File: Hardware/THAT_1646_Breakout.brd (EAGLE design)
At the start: 45.7 x 20.3 mm, 28 parts, among them IC1 THAT1646, J1 1x4, J2 SN, J3 CHASSIS, J4 TN, J5 RN, J6 OUTPUT

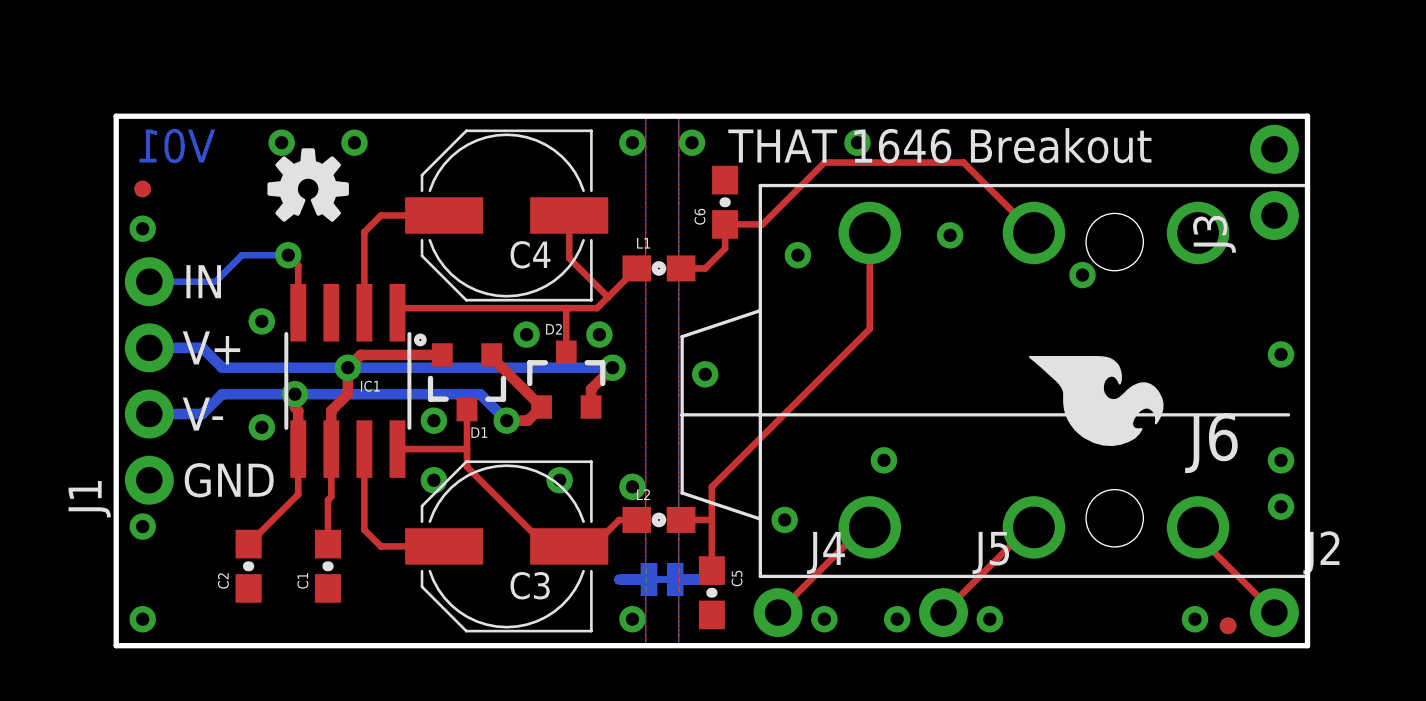
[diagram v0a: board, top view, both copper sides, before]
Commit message: Adding testpoints on T/R/S connections.
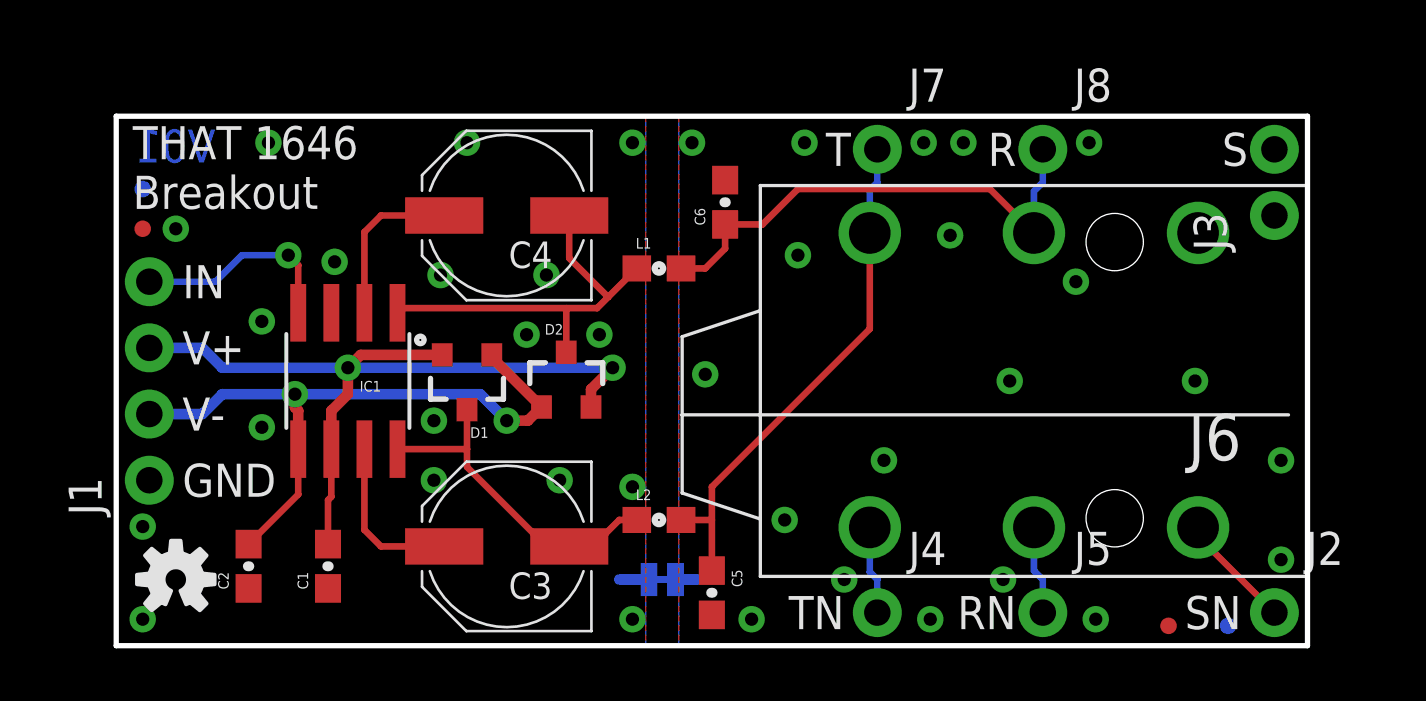
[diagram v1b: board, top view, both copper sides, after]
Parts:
- removed LOGO3: SFE_LOGO_FLAME.2_INCH, SparkFun-Aesthetics:SFE_LOGO_FLAME_.2
- added J7: T, SparkFun-Connectors:1X01_NO_SILK
- added J8: R, SparkFun-Connectors:1X01_NO_SILK
- moved LOGO5 22.4 mm to (17.9, 14.7)
- moved LOGO1 15.8 mm to (2.29, 2.54)
- moved J4 3.81 mm to (29.2, 1.27)
- moved J5 3.81 mm to (35.6, 1.27)
- moved LOGO2 3.39 mm to (4.06, 16.8)
- moved FD4 2.29 mm to (40.4, 0.76)
- moved FD3 1.52 mm to (1.02, 16.0)
- moved LOGO4 1.27 mm to (34.8, 8.64)
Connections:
- net N$8: now also J7.1
- net N$9: now also J8.1
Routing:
- net N$8: track 16.7 -> 20.0 mm
- net N$9: track 16.9 -> 19.4 mm
- net N$2: track 4.87 -> 3.39 mm
- net N$1: track 4.82 -> 3.41 mm
- net GND-ISO: vias 15 -> 20
- net GND: vias 15 -> 18
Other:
- board text added: "R"
- board text added: "S"
- board text added: "T"

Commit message: Moving PTH holes to 0.1 grid.
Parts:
- moved J5 1.27 mm to (36.8, 1.27)
- moved J8 1.27 mm to (36.8, 19.1)
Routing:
- net N$9: track 19.4 -> 19.9 mm
- net N$1: track 3.41 -> 3.94 mm
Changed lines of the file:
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@@
 <setting verticaltext="up"/>
 </settings>
-<grid distance="0.1" unitdist="inch" unit="inch" style="lines" multiple="1" display="yes" altdistance="0.01" altunitdist="inch" altunit="inch"/>
+<grid distance="0.05" unitdist="inch" unit="inch" style="lines" multiple="1" display="yes" altdistance="0.005" altunitdist="inch" altunit="inch"/>
 <layers>
 <layer number="1" name="Top" color="4" fill="1" visible="yes" active="yes"/>
@@
 <layer number="22" name="bPlace" color="14" fill="1" visible="yes" active="yes"/>
 <layer number="23" name="tOrigins" color="15" fill="1" visible="yes" active="yes"/>
-<layer number="24" name="bOrigins" color="15" fill="1" visible="no" active="yes"/>
-<layer number="25" name="tNames" color="7" fill="1" visible="yes" active="yes"/>
+<layer number="24" name="bOrigins" color="15" fill="1" visible="yes" active="yes"/>
+<layer number="25" name="tNames" color="7" fill="1" visible="no" active="yes"/>
 <layer number="26" name="bNames" color="7" fill="1" visible="no" active="yes"/>
 <layer number="27" name="tValues" color="7" fill="1" visible="no" active="yes"/>
@@
 <layer number="43" name="vRestrict" color="2" fill="10" visible="no" active="yes"/>
 <layer number="44" name="Drills" color="7" fill="1" visible="no" active="yes"/>
-<layer number="45" name="Holes" color="7" fill="1" visible="no" active="yes"/>
+<layer number="45" name="Holes" color="7" fill="1" visible="yes" active="yes"/>
 <layer number="46" name="Milling" color="3" fill="1" visible="no" active="yes"/>
-<layer number="47" name="Measures" color="7" fill="1" visible="no" active="yes"/>
+<layer number="47" name="Measures" color="7" fill="1" visible="yes" active="yes"/>
 <layer number="48" name="Document" color="7" fill="1" visible="no" active="yes"/>
 <layer number="49" name="Reference" color="7" fill="1" visible="no" active="yes"/>
 <layer number="50" name="dxf" color="7" fill="1" visible="no" active="no"/>
-<layer number="51" name="tDocu" color="6" fill="1" visible="no" active="yes"/>
+<layer number="51" name="tDocu" color="6" fill="1" visible="yes" active="yes"/>
 <layer number="52" name="bDocu" color="7" fill="1" visible="no" active="yes"/>
 <layer number="53" name="tGND_GNDA" color="7" fill="9" visible="no" active="no"/>
@@
 <text x="2.286" y="6.35" size="1.27" layer="22" font="vector" ratio="15" rot="MR0" align="center-right">GND</text>
 <text x="27.94" y="1.27" size="1.27" layer="22" font="vector" ratio="15" rot="MR180" align="center-right">TN</text>
-<text x="34.29" y="1.27" size="1.27" layer="22" font="vector" ratio="15" rot="MR180" align="center-right">RN</text>
+<text x="35.56" y="1.27" size="1.27" layer="22" font="vector" ratio="15" rot="MR180" align="center-right">RN</text>
 <text x="43.18" y="1.27" size="1.27" layer="22" font="vector" ratio="15" rot="MR180" align="center-right">SN</text>
 <text x="27.94" y="19.05" size="1.27" layer="22" font="vector" ratio="15" rot="MR180" align="center-right">T</text>
-<text x="34.29" y="19.05" size="1.27" layer="22" font="vector" ratio="15" rot="MR180" align="center-right">R</text>
+<text x="35.56" y="19.05" size="1.27" layer="22" font="vector" ratio="15" rot="MR180" align="center-right">R</text>
 <text x="43.18" y="19.05" size="1.27" layer="22" font="vector" ratio="15" rot="MR180" align="center-right">S</text>
 <text x="0.635" y="16.764" size="1.27" layer="21" font="vector" ratio="15">THAT 1646
 Breakout</text>
 <text x="28.194" y="19.05" size="1.27" layer="21" font="vector" ratio="15" align="center-right">T</text>
-<text x="34.544" y="19.05" size="1.27" layer="21" font="vector" ratio="15" align="center-right">R</text>
+<text x="35.814" y="19.05" size="1.27" layer="21" font="vector" ratio="15" align="center-right">R</text>
 <text x="43.434" y="19.05" size="1.27" layer="21" font="vector" ratio="15" align="center-right">S</text>
 <text x="43.18" y="1.27" size="1.27" layer="21" font="vector" ratio="15" align="center-right">SN</text>
-<text x="34.544" y="1.27" size="1.27" layer="21" font="vector" ratio="15" align="center-right">RN</text>
+<text x="35.814" y="1.27" size="1.27" layer="21" font="vector" ratio="15" align="center-right">RN</text>
 <text x="27.94" y="1.27" size="1.27" layer="21" font="vector" ratio="15" align="center-right">TN</text>
 </plain>
@@
 <element name="J2" library="SparkFun-Connectors" package="1X01_NO_SILK" value="SN" x="44.45" y="1.27"/>
 <element name="J4" library="SparkFun-Connectors" package="1X01_NO_SILK" value="TN" x="29.21" y="1.27"/>
-<element name="J5" library="SparkFun-Connectors" package="1X01_NO_SILK" value="RN" x="35.56" y="1.27"/>
+<element name="J5" library="SparkFun-Connectors" package="1X01_NO_SILK" value="RN" x="36.83" y="1.27"/>
 <element name="LOGO4" library="SparkFun-Aesthetics" package="SFE_LOGO_FLAME_.2" value="SFE_LOGO_FLAME.2_INCH" x="34.798" y="8.636" rot="MR90"/>
 <element name="FD1" library="SparkFun-Aesthetics" package="MICRO-FIDUCIAL" value="FIDUCIALUFIDUCIAL" x="1.016" y="17.526" rot="MR0"/>
@@
 </element>
 <element name="J7" library="SparkFun-Connectors" package="1X01_NO_SILK" value="T" x="29.21" y="19.05"/>
-<element name="J8" library="SparkFun-Connectors" package="1X01_NO_SILK" value="R" x="35.56" y="19.05"/>
+<element name="J8" library="SparkFun-Connectors" package="1X01_NO_SILK" value="R" x="36.83" y="19.05"/>
 </elements>
 <signals>
@@
 <via x="26.162" y="14.986" extent="1-16" drill="0.508"/>
 <via x="25.654" y="4.826" extent="1-16" drill="0.508"/>
-<via x="37.592" y="1.016" extent="1-16" drill="0.508"/>
+<via x="38.862" y="1.016" extent="1-16" drill="0.508"/>
 <via x="32.004" y="15.748" extent="1-16" drill="0.508"/>
 <via x="30.988" y="19.304" extent="1-16" drill="0.508"/>
-<via x="32.512" y="19.304" extent="1-16" drill="0.508"/>
-<via x="37.338" y="19.304" extent="1-16" drill="0.508"/>
+<via x="33.782" y="19.304" extent="1-16" drill="0.508"/>
+<via x="38.608" y="19.304" extent="1-16" drill="0.508"/>
 <via x="24.384" y="1.016" extent="1-16" drill="0.508"/>
 <via x="41.402" y="10.16" extent="1-16" drill="0.508"/>
@@
 <wire x1="26.162" y1="17.526" x2="24.804" y2="16.168" width="0.254" layer="1"/>
 <wire x1="35.22" y1="15.84" x2="35.22" y2="17.44" width="0.254" layer="16"/>
-<wire x1="35.22" y1="17.44" x2="35.56" y2="17.78" width="0.254" layer="16"/>
-<wire x1="35.56" y1="17.78" x2="35.56" y2="19.05" width="0.254" layer="16"/>
+<wire x1="35.22" y1="17.44" x2="36.83" y2="19.05" width="0.254" layer="16"/>
 <wire x1="33.534" y1="17.526" x2="35.22" y2="15.84" width="0.254" layer="1"/>
 </signal>
@@
 <contactref element="J5" pad="1"/>
 <wire x1="35.22" y1="4.54" x2="35.22" y2="2.88" width="0.254" layer="16"/>
-<wire x1="35.22" y1="2.88" x2="35.56" y2="2.54" width="0.254" layer="16"/>
-<wire x1="35.56" y1="2.54" x2="35.56" y2="1.27" width="0.254" layer="16"/>
+<wire x1="35.22" y1="2.88" x2="36.83" y2="1.27" width="0.254" layer="16"/>
 </signal>
 <signal name="N$2">
